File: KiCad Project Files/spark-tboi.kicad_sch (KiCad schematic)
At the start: 39 parts, among them IC1 STM32F103C8T7, X1 Y32258MNCCZ

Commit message: revised bom
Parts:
- R5: value 4.7kOhm -> 5.1kOhm
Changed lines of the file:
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@@
 			)
 		)
-		(property "Value" "4.7kOhm"
+		(property "Value" "5.1kOhm"
 			(at 194.5061 132.0799 0)
 			(effects

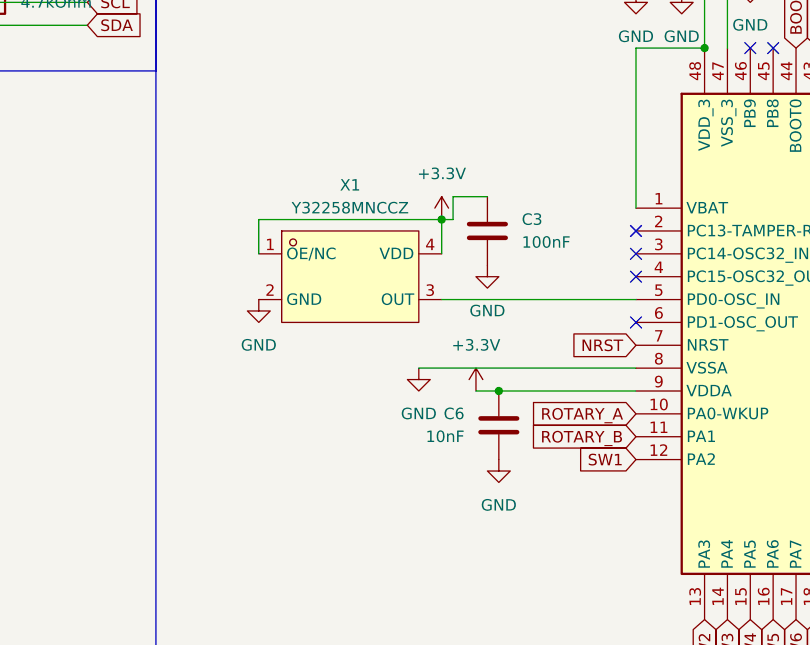
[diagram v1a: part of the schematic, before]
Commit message: Changed distributor to TME
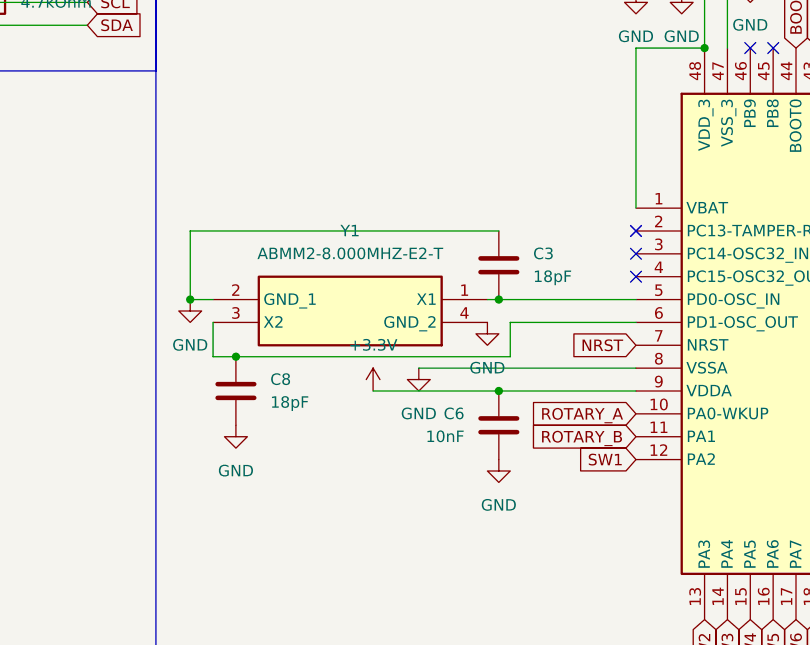
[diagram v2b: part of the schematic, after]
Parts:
- removed C3: 100nF, Capacitor_SMD:C_0603_1608Metric_Pad1.08x0.95mm_HandSolder, symbol REQUIRED:C
- removed X1: Y32258MNCCZ, easyeda2kicad:OSC-SMD_4P-L3.2-W2.5-BL, symbol REQUIRED:Y32258MNCCZ
- added C3, C8: 18pF, Capacitor_SMD:C_0402_1005Metric, symbol REQ:C
- added Y1: ABMM2-8.000MHZ-E2-T, ABMM2, symbol REQ:ABMM2-8.000MHZ-E2-T
- 3V3_LDO1: symbol REQUIRED:AMS1117-3.3_C917183 -> REQ:AMS1117-3.3_C917183
- BOOT_BUTTON1, NRST_BUTTON1: symbol REQUIRED:TS6643TP250GF009 -> REQ:TS6643TP250GF009
- C1, C2, C4, C5, C6, C7: symbol REQUIRED:C -> REQ:C
- CC_TVS1, DATA_TVS1: symbol REQUIRED:RCLAMP0502BATCT -> REQ:RCLAMP0502BATCT
- CH1, CH10, CH11, CH12, CH13, CH14, CH15, CH2, CH3, CH4, CH5, CH6, CH7, CH8, CH9: symbol REQUIRED:KS33_SW_HS_KS-2P02B01-02 -> REQ:KS33_SW_HS_KS-2P02B01-02
- ENCODER1: symbol REQUIRED:RotaryEncoder_Switch -> REQ:RotaryEncoder_Switch
- IC1: symbol REQUIRED:STM32F103C8T7 -> REQ:STM32F103C8T7
- OLED1: symbol REQUIRED:Conn_01x04_Pin -> REQ:Conn_01x04_Pin
- R1, R2, R3, R4, R5: symbol REQUIRED:R -> REQ:R
- UART1: symbol REQUIRED:Conn_01x03_Pin -> REQ:Conn_01x03_Pin
- USB1: symbol REQUIRED:TYPE-C16PIN2MD(073) -> REQ:TYPE-C16PIN2MD(073)
- VBUS_TVS1: symbol REQUIRED:SMBJ5.0A_C83333 -> REQ:SMBJ5.0A_C83333
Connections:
- net GND: now also C3.1, C8.2, Y1.2 (GND_1), Y1.4 (GND_2)
- net at IC1.5 (PD0-OSC_IN): now also C3.2, Y1.1 (X1)
- net at IC1.6 (PD1-OSC_OUT): now also C8.1, Y1.3 (X2)
- no-connect marks 13 -> 12
